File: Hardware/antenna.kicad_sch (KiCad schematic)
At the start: 15 parts, among them J14 252105, J15 252105, J16 252105, J17 J-0530471010, U4 SN74LVC1G14DCKR, U5 HMC544AE

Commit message: Finish schematic v1
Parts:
- renumbered J14 to J18, J15 to J19, J16 to J20, J17 to J21, R85 to R84, R86 to R85, R87 to R86
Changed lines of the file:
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@@
 		(color 0 0 0 0)
 	)
-	(bus_entry
-		(at 82.55 130.81)
-		(size 2.54 2.54)
-		(stroke
-			(width 0)
-			(type default)
-		)
-	)
 	(wire
 		(pts
@@
 		(on_board yes)
 		(dnp no)
-		(property "Reference" "J14"
+		(property "Reference" "J18"
 			(at 80.01 119.38 0)
 			(effects
@@
 			(project "CTS-SAT-2-OBC-PCB"
 				(path "/58243925-df8d-4fc1-899e-fce866d1d25a/368e4a7b-bdab-4813-9da8-67dfcdf79ec2"
-					(reference "J14")
+					(reference "J18")
 					(unit 1)
 				)
@@
 		(on_board yes)
 		(dnp no)
-		(property "Reference" "J16"
+		(property "Reference" "J20"
 			(at 193.04 134.62 0)
 			(effects
@@
 			(project "CTS-SAT-2-OBC-PCB"
 				(path "/58243925-df8d-4fc1-899e-fce866d1d25a/368e4a7b-bdab-4813-9da8-67dfcdf79ec2"
-					(reference "J16")
+					(reference "J20")
 					(unit 1)
 				)
@@
 		(on_board yes)
 		(dnp no)
-		(property "Reference" "R87"
+		(property "Reference" "R86"
 			(at 158.242 144.272 0)
 			(effects
@@
 			(project "CTS-SAT-2-OBC-PCB"
 				(path "/58243925-df8d-4fc1-899e-fce866d1d25a/368e4a7b-bdab-4813-9da8-67dfcdf79ec2"
-					(reference "R87")
+					(reference "R86")
 					(unit 1)
 				)
@@
 		(on_board yes)
 		(dnp no)
-		(property "Reference" "R86"
+		(property "Reference" "R85"
 			(at 155.702 130.302 0)
 			(effects
@@
 			(project "CTS-SAT-2-OBC-PCB"
 				(path "/58243925-df8d-4fc1-899e-fce866d1d25a/368e4a7b-bdab-4813-9da8-67dfcdf79ec2"
-					(reference "R86")
+					(reference "R85")
 					(unit 1)
 				)
@@
 		(on_board yes)
 		(dnp no)
-		(property "Reference" "#PWR0110"
+		(property "Reference" "#PWR0111"
 			(at 186.69 110.49 0)
 			(effects
@@
 			(project "CTS-SAT-2-OBC-PCB"
 				(path "/58243925-df8d-4fc1-899e-fce866d1d25a/368e4a7b-bdab-4813-9da8-67dfcdf79ec2"
-					(reference "#PWR0110")
+					(reference "#PWR0111")
 					(unit 1)
 				)
@@
 		(on_board yes)
 		(dnp no)
-		(property "Reference" "#PWR0111"
+		(property "Reference" "#PWR0112"
 			(at 187.96 147.32 0)
 			(effects
@@
 			(project "CTS-SAT-2-OBC-PCB"
 				(path "/58243925-df8d-4fc1-899e-fce866d1d25a/368e4a7b-bdab-4813-9da8-67dfcdf79ec2"
-					(reference "#PWR0111")
+					(reference "#PWR0112")
 					(unit 1)
 				)
@@
 		(on_board yes)
 		(dnp no)
-		(property "Reference" "J17"
+		(property "Reference" "J21"
 			(at 295.656 82.296 0)
 			(effects
@@
 			(project "CTS-SAT-2-OBC-PCB"
 				(path "/58243925-df8d-4fc1-899e-fce866d1d25a/368e4a7b-bdab-4813-9da8-67dfcdf79ec2"
-					(reference "J17")
+					(reference "J21")
 					(unit 1)
 				)
@@
 		(on_board yes)
 		(dnp no)
-		(property "Reference" "#PWR0102"
+		(property "Reference" "#PWR0103"
 			(at 95.25 143.51 0)
 			(effects
@@
 			(project "CTS-SAT-2-OBC-PCB"
 				(path "/58243925-df8d-4fc1-899e-fce866d1d25a/368e4a7b-bdab-4813-9da8-67dfcdf79ec2"
-					(reference "#PWR0102")
+					(reference "#PWR0103")
 					(unit 1)
 				)
@@
 		(on_board yes)
 		(dnp no)
-		(property "Reference" "#PWR0101"
+		(property "Reference" "#PWR0102"
 			(at 85.09 160.02 0)
 			(effects
@@
 			(project "CTS-SAT-2-OBC-PCB"
 				(path "/58243925-df8d-4fc1-899e-fce866d1d25a/368e4a7b-bdab-4813-9da8-67dfcdf79ec2"
-					(reference "#PWR0101")
+					(reference "#PWR0102")
 					(unit 1)
 				)
@@
 		(on_board yes)
 		(dnp no)
-		(property "Reference" "#PWR0103"
+		(property "Reference" "#PWR0104"
 			(at 110.49 110.49 0)
 			(effects
@@
 			(project "CTS-SAT-2-OBC-PCB"
 				(path "/58243925-df8d-4fc1-899e-fce866d1d25a/368e4a7b-bdab-4813-9da8-67dfcdf79ec2"
-					(reference "#PWR0103")
+					(reference "#PWR0104")
 					(unit 1)
 				)
@@
 		(on_board yes)
 		(dnp no)
-		(property "Reference" "#PWR0108"
+		(property "Reference" "#PWR0109"
 			(at 157.48 153.67 0)
 			(effects
@@
 			(project "CTS-SAT-2-OBC-PCB"
 				(path "/58243925-df8d-4fc1-899e-fce866d1d25a/368e4a7b-bdab-4813-9da8-67dfcdf79ec2"
-					(reference "#PWR0108")
+					(reference "#PWR0109")
 					(unit 1)
 				)
@@
 		(on_board yes)
 		(dnp no)
-		(property "Reference" "R85"
+		(property "Reference" "R84"
 			(at 113.03 93.98 0)
 			(effects
@@
 			(project "CTS-SAT-2-OBC-PCB"
 				(path "/58243925-df8d-4fc1-899e-fce866d1d25a/368e4a7b-bdab-4813-9da8-67dfcdf79ec2"
-					(reference "R85")
+					(reference "R84")
 					(unit 1)
 				)
@@
 		(on_board yes)
 		(dnp no)
-		(property "Reference" "#PWR0109"
+		(property "Reference" "#PWR0110"
 			(at 186.69 100.33 0)
 			(effects
@@
 			(project "CTS-SAT-2-OBC-PCB"
 				(path "/58243925-df8d-4fc1-899e-fce866d1d25a/368e4a7b-bdab-4813-9da8-67dfcdf79ec2"
-					(reference "#PWR0109")
+					(reference "#PWR0110")
 					(unit 1)
 				)
@@
 		(on_board yes)
 		(dnp no)
-		(property "Reference" "J15"
+		(property "Reference" "J19"
 			(at 81.28 147.32 0)
 			(effects
@@
 			(project "CTS-SAT-2-OBC-PCB"
 				(path "/58243925-df8d-4fc1-899e-fce866d1d25a/368e4a7b-bdab-4813-9da8-67dfcdf79ec2"
-					(reference "J15")
+					(reference "J19")
 					(unit 1)
 				)
@@
 		(dnp no)
 		(fields_autoplaced yes)
-		(property "Reference" "#PWR0112"
+		(property "Reference" "#PWR0113"
 			(at 265.43 116.84 0)
 			(effects
@@
 			(project "CTS-SAT-2-OBC-PCB"
 				(path "/58243925-df8d-4fc1-899e-fce866d1d25a/368e4a7b-bdab-4813-9da8-67dfcdf79ec2"
-					(reference "#PWR0112")
+					(reference "#PWR0113")
 					(unit 1)
 				)
@@
 		(on_board yes)
 		(dnp no)
-		(property "Reference" "#PWR0100"
+		(property "Reference" "#PWR0101"
 			(at 83.82 132.08 0)
 			(effects
@@
 			(project "CTS-SAT-2-OBC-PCB"
 				(path "/58243925-df8d-4fc1-899e-fce866d1d25a/368e4a7b-bdab-4813-9da8-67dfcdf79ec2"
-					(reference "#PWR0100")
+					(reference "#PWR0101")
 					(unit 1)
 				)
@@
 		(on_board yes)
 		(dnp no)
-		(property "Reference" "#PWR0107"
+		(property "Reference" "#PWR0108"
 			(at 154.94 120.65 0)
 			(effects
@@
 			(project "CTS-SAT-2-OBC-PCB"
 				(path "/58243925-df8d-4fc1-899e-fce866d1d25a/368e4a7b-bdab-4813-9da8-67dfcdf79ec2"
-					(reference "#PWR0107")
+					(reference "#PWR0108")
 					(unit 1)
 				)
@@
 		(on_board yes)
 		(dnp no)
-		(property "Reference" "#PWR0105"
+		(property "Reference" "#PWR0106"
 			(at 146.05 120.65 0)
 			(effects
@@
 			(project "CTS-SAT-2-OBC-PCB"
 				(path "/58243925-df8d-4fc1-899e-fce866d1d25a/368e4a7b-bdab-4813-9da8-67dfcdf79ec2"
-					(reference "#PWR0105")
+					(reference "#PWR0106")
 					(unit 1)
 				)
@@
 		(on_board yes)
 		(dnp no)
-		(property "Reference" "#PWR0104"
+		(property "Reference" "#PWR0105"
 			(at 125.73 110.49 0)
 			(effects
@@
 			(project "CTS-SAT-2-OBC-PCB"
 				(path "/58243925-df8d-4fc1-899e-fce866d1d25a/368e4a7b-bdab-4813-9da8-67dfcdf79ec2"
-					(reference "#PWR0104")
+					(reference "#PWR0105")
 					(unit 1)
 				)
@@
 		(on_board yes)
 		(dnp no)
-		(property "Reference" "#PWR0106"
+		(property "Reference" "#PWR0107"
 			(at 146.05 153.67 0)
 			(effects
@@
 			(project "CTS-SAT-2-OBC-PCB"
 				(path "/58243925-df8d-4fc1-899e-fce866d1d25a/368e4a7b-bdab-4813-9da8-67dfcdf79ec2"
-					(reference "#PWR0106")
+					(reference "#PWR0107")
 					(unit 1)
 				)

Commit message: Assign footprints
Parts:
- C43, C44, C45, C46, C47, C48: footprint 0603 -> Capacitor_SMD:C_0603_1608Metric
- J18, J19, J20: footprint J-252105 -> CTS-SAT-1:J-252105
- J21: footprint J-0530471010 -> CTS-SAT-1:J-0530471010
- R84, R85, R86: footprint 0603 -> Resistor_SMD:R_0603_1608Metric
- U4: footprint U-SN74LVC1G14DCKR -> CTS-SAT-1:U-SN74LVC1G14DCKR
- U5: footprint U-HMC544AETR -> CTS-SAT-1:U-HMC544AETR
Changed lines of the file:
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@@
 			)
 		)
-		(property "Footprint" "J-252105"
+		(property "Footprint" "CTS-SAT-1:J-252105"
 			(at 74.93 124.46 0)
 			(effects
@@
 			)
 		)
-		(property "Footprint" "J-252105"
+		(property "Footprint" "CTS-SAT-1:J-252105"
 			(at 196.85 139.7 0)
 			(effects
@@
 			)
 		)
-		(property "Footprint" "0603"
+		(property "Footprint" "Resistor_SMD:R_0603_1608Metric"
 			(at 157.48 146.05 0)
 			(effects
@@
 			)
 		)
-		(property "Footprint" "0603"
+		(property "Footprint" "Capacitor_SMD:C_0603_1608Metric"
 			(at 146.05 134.62 0)
 			(effects
@@
 			)
 		)
-		(property "Footprint" "U-HMC544AETR"
+		(property "Footprint" "CTS-SAT-1:U-HMC544AETR"
 			(at 123.19 137.16 0)
 			(effects
@@
 			)
 		)
-		(property "Footprint" "0603"
+		(property "Footprint" "Resistor_SMD:R_0603_1608Metric"
 			(at 154.94 132.08 0)
 			(effects
@@
 			)
 		)
-		(property "Footprint" "0603"
+		(property "Footprint" "Capacitor_SMD:C_0603_1608Metric"
 			(at 177.8 137.16 0)
 			(effects
@@
 			)
 		)
-		(property "Footprint" "J-0530471010"
+		(property "Footprint" "CTS-SAT-1:J-0530471010"
 			(at 295.91 95.25 0)
 			(effects
@@
 			)
 		)
-		(property "Footprint" "0603"
+		(property "Footprint" "Capacitor_SMD:C_0603_1608Metric"
 			(at 91.44 149.86 0)
 			(effects
@@
 			)
 		)
-		(property "Footprint" "0603"
+		(property "Footprint" "Capacitor_SMD:C_0603_1608Metric"
 			(at 90.17 121.92 0)
 			(effects
@@
 			)
 		)
-		(property "Footprint" "U-SN74LVC1G14DCKR"
+		(property "Footprint" "CTS-SAT-1:U-SN74LVC1G14DCKR"
 			(at 95.25 99.06 0)
 			(effects
@@
 			)
 		)
-		(property "Footprint" "0603"
+		(property "Footprint" "Resistor_SMD:R_0603_1608Metric"
 			(at 109.22 93.98 0)
 			(effects
@@
 			)
 		)
-		(property "Footprint" "J-252105"
+		(property "Footprint" "CTS-SAT-1:J-252105"
 			(at 76.2 152.4 0)
 			(effects
@@
 			)
 		)
-		(property "Footprint" "0603"
+		(property "Footprint" "Capacitor_SMD:C_0603_1608Metric"
 			(at 146.05 147.32 0)
 			(effects
@@
 			)
 		)
-		(property "Footprint" "0603"
+		(property "Footprint" "Capacitor_SMD:C_0603_1608Metric"
 			(at 186.69 104.14 0)
 			(effects

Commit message: Comms
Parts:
- removed R84: 100K, Resistor_SMD:R_0603_1608Metric, symbol OBC Development Board:root_0_RT-100K0-F-1/16W-0603_OBC Development Board.SchLib
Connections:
- no-connect marks 0 -> 1
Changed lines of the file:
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@@
 		(color 0 0 0 0)
 	)
+	(no_connect
+		(at 125.73 93.98)
+	)
 	(wire
 		(pts
@@
 	(wire
 		(pts
-			(xy 125.73 93.98) (xy 120.65 93.98)
-		)
-		(stroke
-			(width 0)
-			(type default)
-		)
-	)
-	(wire
-		(pts
 			(xy 143.51 134.62) (xy 146.05 134.62)
 		)
@@
 	(wire
 		(pts
-			(xy 115.57 93.98) (xy 110.49 93.98)
-		)
-		(stroke
-			(width 0)
-			(type default)
-		)
-	)
-	(wire
-		(pts
 			(xy 173.99 101.6) (xy 173.99 139.7)
 		)
@@
 		(pts
 			(xy 283.21 87.63) (xy 290.83 87.63)
-		)
-		(stroke
-			(width 0)
-			(type default)
-		)
-	)
-	(wire
-		(pts
-			(xy 110.49 93.98) (xy 110.49 104.14)
 		)
 		(stroke
@@
 	)
 	(symbol
-		(lib_id "power:GND")
-		(at 110.49 104.14 0)
-		(unit 1)
-		(exclude_from_sim no)
-		(in_bom yes)
-		(on_board yes)
-		(dnp no)
-		(property "Reference" "#PWR0104"
-			(at 110.49 110.49 0)
-			(effects
-				(font
-					(size 1.27 1.27)
-				)
-				(hide yes)
-			)
-		)
-		(property "Value" "GND"
-			(at 110.49 107.95 0)
-			(effects
-				(font
-					(size 1.27 1.27)
-				)
-			)
-		)
-		(property "Footprint" ""
-			(at 110.49 104.14 0)
-			(effects
-				(font
-					(size 1.27 1.27)
-				)
-				(hide yes)
-			)
-		)
-		(property "Datasheet" ""
-			(at 110.49 104.14 0)
-			(effects
-				(font
-					(size 1.27 1.27)
-				)
-				(hide yes)
-			)
-		)
-		(property "Description" "Power symbol creates a global label with name \"GND\" , ground"
-			(at 110.49 104.14 0)
-			(effects
-				(font
-					(size 1.27 1.27)
-				)
-				(hide yes)
-			)
-		)
-		(pin "1"
-		)
-		(instances
-			(project "CTS-SAT-2-OBC-PCB"
-				(path "/58243925-df8d-4fc1-899e-fce866d1d25a/368e4a7b-bdab-4813-9da8-67dfcdf79ec2"
-					(reference "#PWR0104")
-					(unit 1)
-				)
-			)
-		)
-	)
-	(symbol
 		(lib_id "RS2D:root_0_CC-108-K-50V-X7R-0603_RS2D.SchLib")
 		(at 91.44 149.86 0)
@@
 					(unit 1)
 				)
-			)
-		)
-	)
-	(symbol
-		(lib_id "OBC Development Board:root_0_RT-100K0-F-1/16W-0603_OBC Development Board.SchLib")
-		(at 109.22 93.98 0)
-		(unit 1)
-		(exclude_from_sim no)
-		(in_bom yes)
-		(on_board yes)
-		(dnp no)
-		(property "Reference" "R84"
-			(at 113.03 93.98 0)
-			(effects
-				(font
-					(size 1.27 1.27)
-				)
-				(justify left bottom)
-			)
-		)
-		(property "Value" "100K"
-			(at 109.22 93.98 0)
-			(effects
-				(font
-					(size 1.27 1.27)
-				)
-				(justify left bottom)
-				(hide yes)
-			)
-		)
-		(property "Footprint" "Resistor_SMD:R_0603_1608Metric"
-			(at 109.22 93.98 0)
-			(effects
-				(font
-					(size 1.27 1.27)
-				)
-				(hide yes)
-			)
-		)
-		(property "Datasheet" ""
-			(at 109.22 93.98 0)
-			(effects
-				(font
-					(size 1.27 1.27)
-				)
-				(hide yes)
-			)
-		)
-		(property "Description" "RES SMD 100KΩ 0.1% 1/16W 0603"
-			(at 109.22 93.98 0)
-			(effects
-				(font
-					(size 1.27 1.27)
-				)
-				(hide yes)
-			)
-		)
-		(property "COMPONENTLINK2URL" "https://www.te.com/commerce/DocumentDelivery/DDEController?Action=showdoc&DocId=Data+Sheet%7F1773200%7FM%7Fpdf%7FEnglish%7FENG_DS_1773200_M.pdf%7F3-1676481-2"
-			(at 108.712 91.44 0)
-			(effects
-				(font
-					(size 1.27 1.27)
-				)
-				(justify left bottom)
-				(hide yes)
-			)
-		)
-		(property "COMPONENTLINK2DESCRIPTION" "Datasheet"
-			(at 108.712 91.44 0)
-			(effects
-				(font
-					(size 1.27 1.27)
-				)
-				(justify left bottom)
-				(hide yes)
-			)
-		)
-		(property "DISTRIBUTOR" "Digikey"
-			(at 113.03 97.282 0)
-			(effects
-				(font
-					(size 1.27 1.27)
-				)
-				(justify left bottom)
-				(hide yes)
-			)
-		)
-		(property "DISTRIBUTOR PART #" "A119912CT-ND"
-			(at 113.03 97.282 0)
-			(effects
-				(font
-					(size 1.27 1.27)
-				)
-				(justify left bottom)
-				(hide yes)
-			)
-		)
-		(property "MANUFACTURER" "TE Connectivity"
-			(at 113.03 97.282 0)
-			(effects
-				(font
-					(size 1.27 1.27)
-				)
-				(justify left bottom)
-				(hide yes)
-			)
-		)
-		(property "MANUFACTURER PART #" "CPF0603B100KE"
-			(at 113.03 97.282 0)
-			(effects
-				(font
-					(size 1.27 1.27)
-				)
-				(justify left bottom)
-				(hide yes)
-			)
-		)
-		(property "PART DESCRIPTION" "RES SMD 100KΩ 0.1% 1/16W 0603"
-			(at 113.03 97.282 0)
-			(effects
-				(font
-					(size 1.27 1.27)
-				)
-				(justify left bottom)
-				(hide yes)
-			)
-		)
-		(property "ALTIUM_VALUE" "100K"
-			(at 113.03 97.282 0)
-			(effects
-				(font
-					(size 1.27 1.27)
-				)
-				(justify left bottom)
-				(hide yes)
-			)
-		)
-		(pin "1"
-		)
-		(pin "2"
-		)
-		(instances
-			(project "CTS-SAT-2-OBC-PCB"
-				(path "/58243925-df8d-4fc1-899e-fce866d1d25a/368e4a7b-bdab-4813-9da8-67dfcdf79ec2"
-					(reference "R84")
-					(unit 1)
-				)

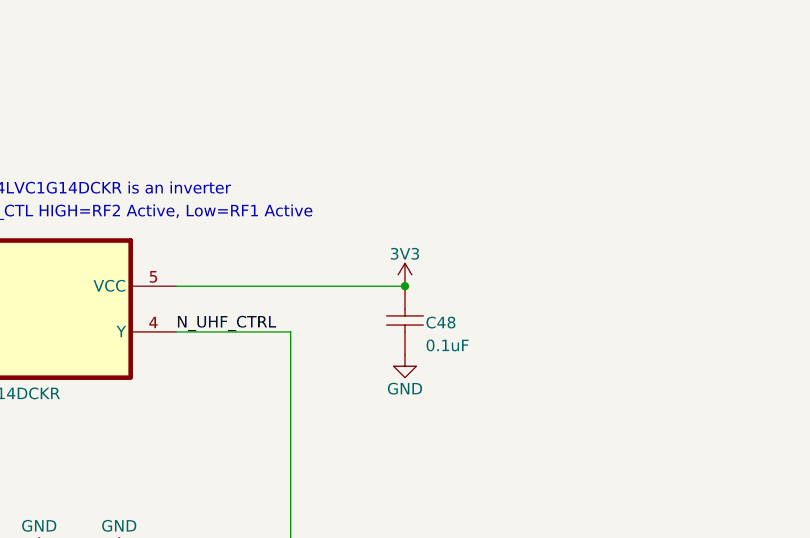
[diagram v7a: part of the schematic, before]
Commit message: Reroute power
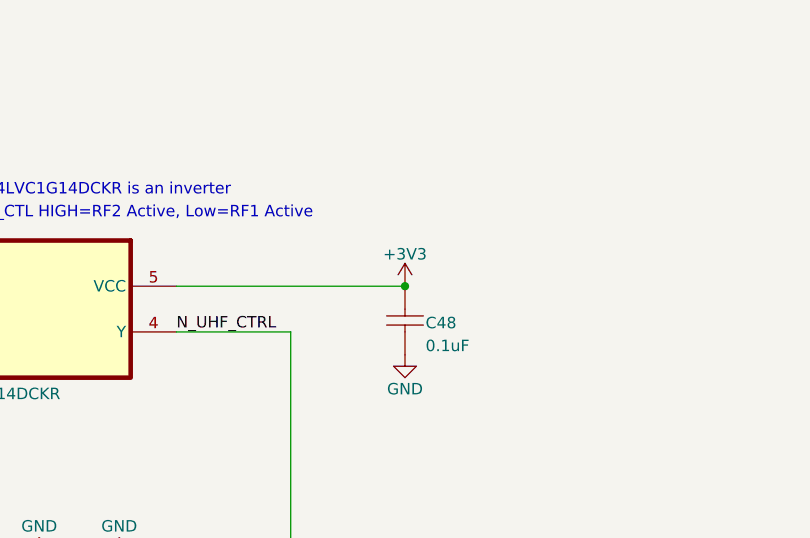
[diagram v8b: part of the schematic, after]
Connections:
- net 3V3 renamed +3V3
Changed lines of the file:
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@@
 			)
 		)
-		(property "Value" "3V3"
+		(property "Value" "+3V3"
 			(at 186.69 92.964 0)
 			(effects
